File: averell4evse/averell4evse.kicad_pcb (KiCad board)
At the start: 2 copper layers, 91 x 78 mm, 43 parts, among them J1 Conn_01x16, J2 Conn_01x13, J3 Conn_01x04, J4 Conn_01x03, J5 Conn_01x09, U1 KT2520K-T, U2 NFCv4, U3 TLC5957RTQ, U4 74AUC2G125, U5 touch_sensor

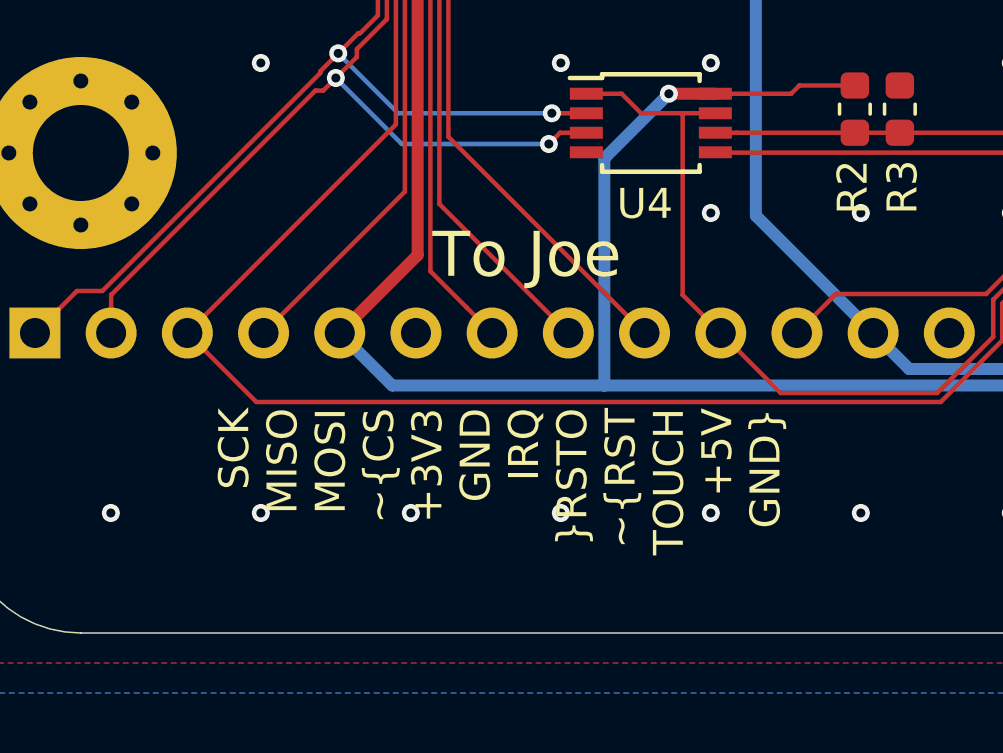
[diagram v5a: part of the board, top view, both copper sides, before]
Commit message: averell/pcb: Add DRV_CS to Joe connector silkscreen
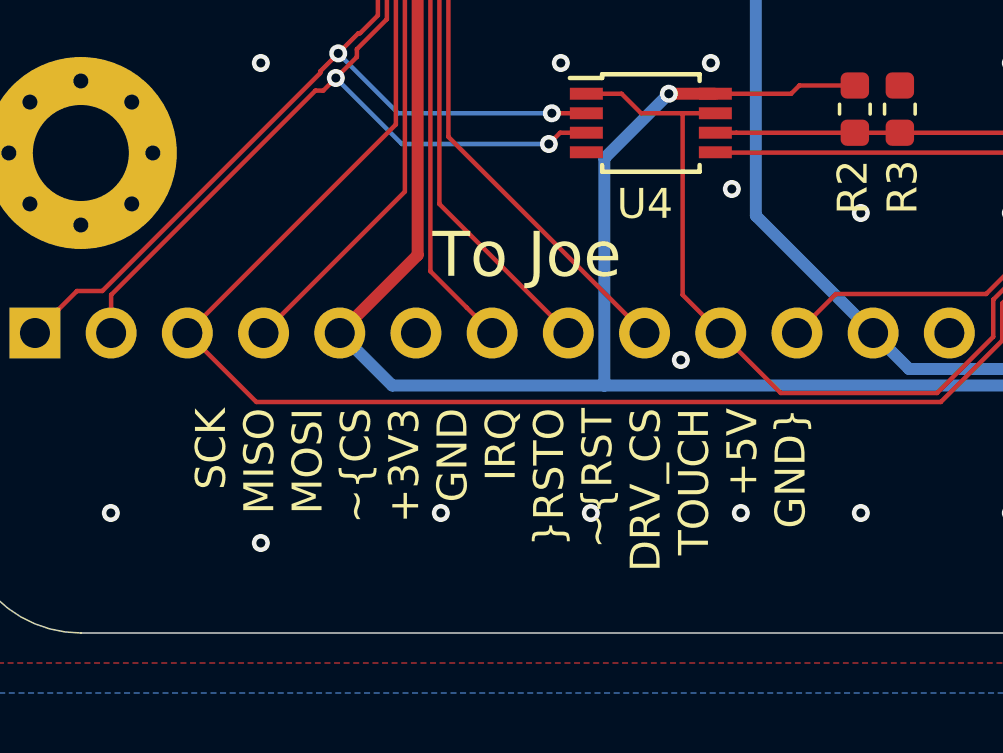
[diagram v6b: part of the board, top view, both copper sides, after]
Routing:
- net GND: vias 97 -> 98
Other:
- board text added: "SCK MISO MOSI ~CS +3V3 GND IRQ ~RSTO ~RST DRV_CS TOUCH +5V GND"
- board text removed: "SCK MISO MOSI ~CS +3V3 GND IRQ ~RSTO ~RST TOUCH +5V GND"
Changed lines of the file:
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@@
     (thickness 1.6)
     (drawings 35)
-    (tracks 1123)
+    (tracks 1124)
     (zones 0)
     (modules 44)
@@
     (effects (font (size 1 1) (thickness 0.15)) (justify right))
   )
-  (gr_text "SCK\nMISO\nMOSI\n~CS\n+3V3\nGND\nIRQ\n~RSTO\n~RST\nTOUCH\n+5V\nGND" (at 92.97 117.7 90) (layer B.SilkS)
+  (gr_text "SCK\nMISO\nMOSI\n~CS\n+3V3\nGND\nIRQ\n~RSTO\n~RST\nDRV_CS\nTOUCH\n+5V\nGND" (at 92.97 117.7 90) (layer B.SilkS)
     (effects (font (size 1 1) (thickness 0.15)) (justify right mirror))
   )
-  (gr_text "SCK\nMISO\nMOSI\n~CS\n+3V3\nGND\nIRQ\n~RSTO\n~RST\nTOUCH\n+5V\nGND" (at 92.97 121.5 90) (layer F.SilkS)
+  (gr_text "SCK\nMISO\nMOSI\n~CS\n+3V3\nGND\nIRQ\n~RSTO\n~RST\nDRV_CS\nTOUCH\n+5V\nGND" (at 93 121.5 90) (layer F.SilkS)
     (effects (font (size 1 1) (thickness 0.15)) (justify right))
   )
@@
   (via (at 146.17 115) (size 0.6) (drill 0.3) (layers F.Cu B.Cu) (net 1))
   (via (at 155.2 117) (size 0.6) (drill 0.3) (layers F.Cu B.Cu) (net 1))
-  (via (at 151.5 119.2) (size 0.6) (drill 0.3) (layers F.Cu B.Cu) (net 28))
   (via (at 150.5 94.6) (size 0.6) (drill 0.3) (layers F.Cu B.Cu) (net 1))
   (via (at 154.5 90.2) (size 0.6) (drill 0.3) (layers F.Cu B.Cu) (net 1))
@@
   (via (at 145 110) (size 0.6) (drill 0.3) (layers F.Cu B.Cu) (net 1))
   (via (at 140 110) (size 0.6) (drill 0.3) (layers F.Cu B.Cu) (net 1))
-  (via (at 100 115) (size 0.6) (drill 0.3) (layers F.Cu B.Cu) (net 1))
+  (via (at 100.7 114.2) (size 0.6) (drill 0.3) (layers F.Cu B.Cu) (net 1))
   (via (at 105 115) (size 0.6) (drill 0.3) (layers F.Cu B.Cu) (net 1))
   (via (at 110 115) (size 0.6) (drill 0.3) (layers F.Cu B.Cu) (net 1))
@@
   (via (at 165 120) (size 0.6) (drill 0.3) (layers F.Cu B.Cu) (net 1))
   (via (at 80 125) (size 0.6) (drill 0.3) (layers F.Cu B.Cu) (net 1))
-  (via (at 85 125) (size 0.6) (drill 0.3) (layers F.Cu B.Cu) (net 1))
-  (via (at 95 125) (size 0.6) (drill 0.3) (layers F.Cu B.Cu) (net 1))
-  (via (at 90 125) (size 0.6) (drill 0.3) (layers F.Cu B.Cu) (net 1))
-  (via (at 100 125) (size 0.6) (drill 0.3) (layers F.Cu B.Cu) (net 1))
+  (via (at 85 126) (size 0.6) (drill 0.3) (layers F.Cu B.Cu) (net 1))
+  (via (at 96 125) (size 0.6) (drill 0.3) (layers F.Cu B.Cu) (net 1))
+  (via (at 91 125) (size 0.6) (drill 0.3) (layers F.Cu B.Cu) (net 1))
+  (via (at 101 125) (size 0.6) (drill 0.3) (layers F.Cu B.Cu) (net 1))
   (via (at 105 125) (size 0.6) (drill 0.3) (layers F.Cu B.Cu) (net 1))
   (via (at 110 125) (size 0.6) (drill 0.3) (layers F.Cu B.Cu) (net 1))
@@
   (via (at 85 105) (size 0.6) (drill 0.3) (layers F.Cu B.Cu) (net 1))
   (via (at 85 110) (size 0.6) (drill 0.3) (layers F.Cu B.Cu) (net 1))
+  (via (at 99 119.9) (size 0.6) (drill 0.3) (layers F.Cu B.Cu) (net 1))
   (via (at 129 111.2) (size 0.6) (drill 0.3) (layers F.Cu B.Cu) (net 2))
   (segment (start 129 111.2) (end 129 112.2125) (width 0.4) (layer F.Cu) (net 2))
@@
   (segment (start 99.4 97.75) (end 99.925001 97.224999) (width 0.15) (layer B.Cu) (net 27))
   (segment (start 98.5 97.75) (end 99.4 97.75) (width 0.15) (layer B.Cu) (net 27))
+  (via (at 151.5 119.2) (size 0.6) (drill 0.3) (layers F.Cu B.Cu) (net 28))
   (segment (start 132.75 110.281602) (end 132.75 109.9375) (width 0.15) (layer F.Cu) (net 28))
   (segment (start 132.55001 110.481592) (end 132.75 110.281602) (width 0.15) (layer F.Cu) (net 28))
@@
   (segment (start 101.38 88.7) (end 99.2 90.88) (width 0.15) (layer F.Cu) (net 44))
   (segment (start 99.2 90.88) (end 99.2 91.794334) (width 0.15) (layer F.Cu) (net 44))
-  (via (at 130.25 99.6) (size 0.6) (drill 0.3) (layers F.Cu B.Cu) (net 77))
-  (segment (start 130.25 101.525) (end 130.25 99.6) (width 0.15) (layer F.Cu) (net 77))
-  (segment (start 130.25 102.0625) (end 130.25 101.525) (width 0.15) (layer F.Cu) (net 77))
   (via (at 130.775 100.157472) (size 0.6) (drill 0.3) (layers F.Cu B.Cu) (net 45))
   (segment (start 130.75 102.0625) (end 130.75 100.182472) (width 0.15) (layer F.Cu) (net 45))
@@
   (segment (start 87.5 110.5) (end 87.08 110.92) (width 0.15) (layer F.Cu) (net 46))
   (segment (start 87.08 110.92) (end 86.82 110.92) (width 0.15) (layer F.Cu) (net 46))
-  (via (at 129.725 100.176167) (size 0.6) (drill 0.3) (layers F.Cu B.Cu) (net 78))
-  (segment (start 129.75 102.0625) (end 129.75 100.201167) (width 0.15) (layer F.Cu) (net 78))
-  (segment (start 129.75 100.201167) (end 129.725 100.176167) (width 0.15) (layer F.Cu) (net 78))
-  (via (at 125.3 106.3) (size 0.6) (drill 0.3) (layers F.Cu B.Cu) (net 78))
-  (segment (start 125.3 106.3) (end 125.3 104.248443) (width 0.15) (layer B.Cu) (net 78))
-  (segment (start 125.3 104.248443) (end 129.024222 100.524221) (width 0.15) (layer B.Cu) (net 78))
-  (segment (start 129.376946 100.524221) (end 129.725 100.176167) (width 0.15) (layer B.Cu) (net 78))
-  (segment (start 129.024222 100.524221) (end 129.376946 100.524221) (width 0.15) (layer B.Cu) (net 78))
   (segment (start 93.76 95.9615) (end 93.76 88.7) (width 0.15) (layer F.Cu) (net 47))
   (segment (start 88.89999 100.821512) (end 88.901519 100.819981) (width 0.15) (layer F.Cu) (net 47))
@@
   (segment (start 96.535 64.5) (end 96.535 56.065) (width 0.15) (layer B.Cu) (net 76))
   (segment (start 96.535 56.065) (end 97.774989 54.825011) (width 0.15) (layer B.Cu) (net 76))
+  (via (at 130.25 99.6) (size 0.6) (drill 0.3) (layers F.Cu B.Cu) (net 77))
+  (segment (start 130.25 101.525) (end 130.25 99.6) (width 0.15) (layer F.Cu) (net 77))
+  (segment (start 130.25 102.0625) (end 130.25 101.525) (width 0.15) (layer F.Cu) (net 77))
   (segment (start 99.06 111.675) (end 100.15 111.675) (width 0.15) (layer F.Cu) (net 77))
   (segment (start 130.25 99.6) (end 129.524165 99.6) (width 0.15) (layer B.Cu) (net 77))
@@
   (segment (start 99.06 117.73) (end 99.06 111.675) (width 0.15) (layer F.Cu) (net 77))
   (segment (start 100.33 119) (end 99.06 117.73) (width 0.15) (layer F.Cu) (net 77))
+  (via (at 129.725 100.176167) (size 0.6) (drill 0.3) (layers F.Cu B.Cu) (net 78))
+  (segment (start 129.75 102.0625) (end 129.75 100.201167) (width 0.15) (layer F.Cu) (net 78))
+  (segment (start 129.75 100.201167) (end 129.725 100.176167) (width 0.15) (layer F.Cu) (net 78))
+  (via (at 125.3 106.3) (size 0.6) (drill 0.3) (layers F.Cu B.Cu) (net 78))
+  (segment (start 125.3 106.3) (end 125.3 104.248443) (width 0.15) (layer B.Cu) (net 78))
+  (segment (start 125.3 104.248443) (end 129.024222 100.524221) (width 0.15) (layer B.Cu) (net 78))
+  (segment (start 129.376946 100.524221) (end 129.725 100.176167) (width 0.15) (layer B.Cu) (net 78))
+  (segment (start 129.024222 100.524221) (end 129.376946 100.524221) (width 0.15) (layer B.Cu) (net 78))
   (segment (start 100.85 112.325) (end 104.8 112.325) (width 0.15) (layer F.Cu) (net 78))
   (segment (start 100.15 112.325) (end 100.85 112.325) (width 0.15) (layer F.Cu) (net 78))

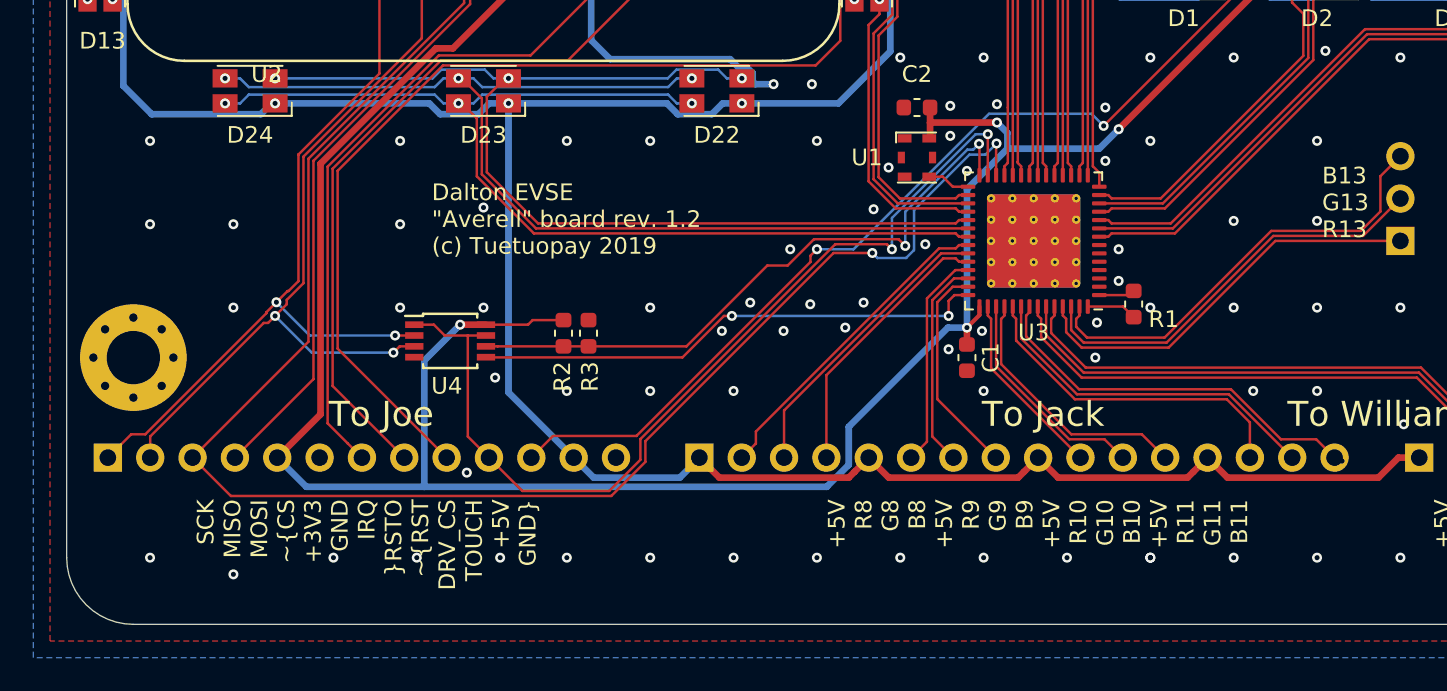
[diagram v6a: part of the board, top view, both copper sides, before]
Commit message: averell/pcb: Replace Joe connector with RJ45 jacks
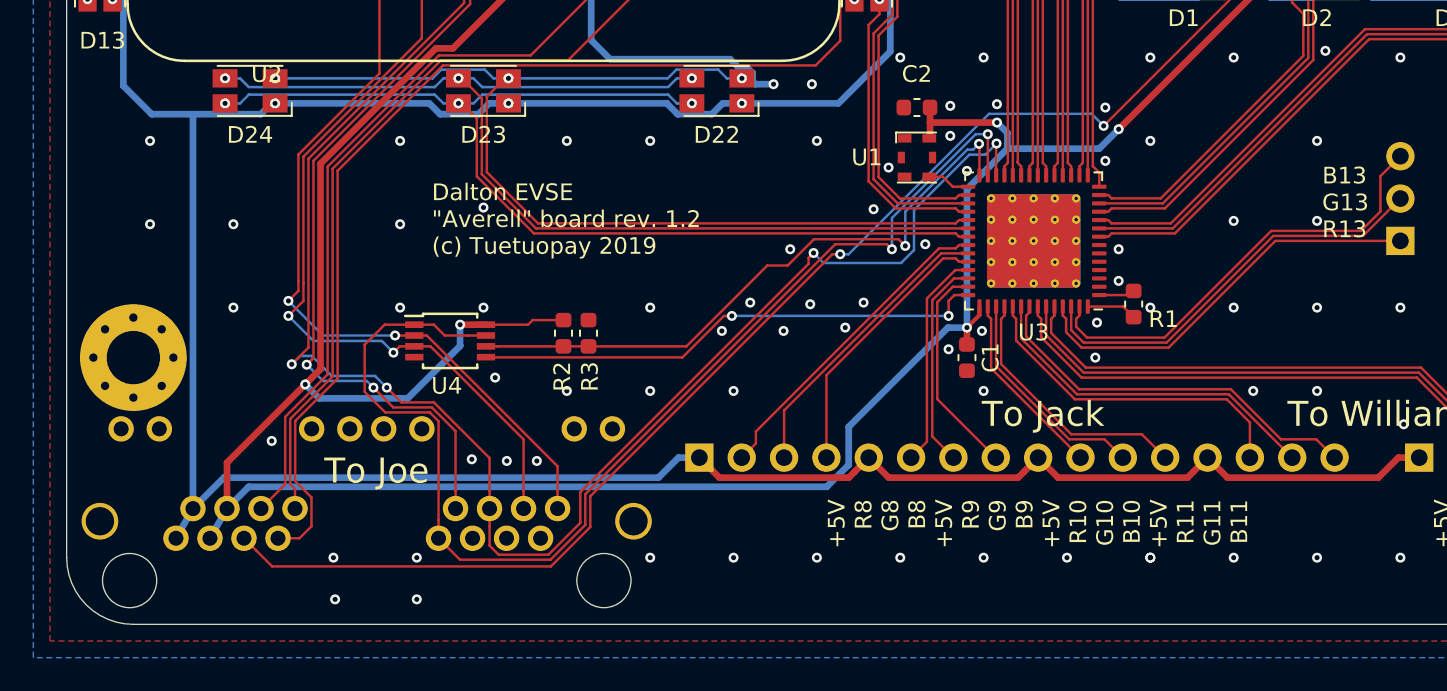
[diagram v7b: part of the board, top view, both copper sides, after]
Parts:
- J2: value Conn_01x13 -> CONNFLY_Elec_DS1129-04-S8B0P-X; footprint Connector_PinHeader_2.54mm:PinHeader_1x13_P2.54mm_Horizontal -> ma4evse:CONNFLY_Elec_DS1129-04-S8B0P-X
- moved J2 16.3 mm to (93.0, 124.0), turned to 180 degrees
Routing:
- net +5V: track 358.3 -> 384.2 mm
- net /TOUCH: track 61.8 -> 83.3 mm
- net /DRV_CS: track 56.6 -> 72.0 mm
- net +3V3: track 174.4 -> 185.2 mm, vias 4 -> 5
- net /NFC_CS: track 37.0 -> 44.9 mm, vias 0 -> 2
- net /~RST: track 94.6 -> 99.8 mm
- net /MOSI: track 99.3 -> 94.8 mm, vias 2 -> 4
- net /IRQ: track 42.0 -> 45.8 mm
- net /~RSTO: track 45.1 -> 47.5 mm
- net /SCK: track 46.7 -> 46.0 mm
- net GND: vias 98 -> 99
- net /B11: vias 1 -> 0
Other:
- board text removed: "SCK MISO MOSI ~CS +3V3 GND IRQ ~RSTO ~RST DRV_CS TOUCH +5V GND"

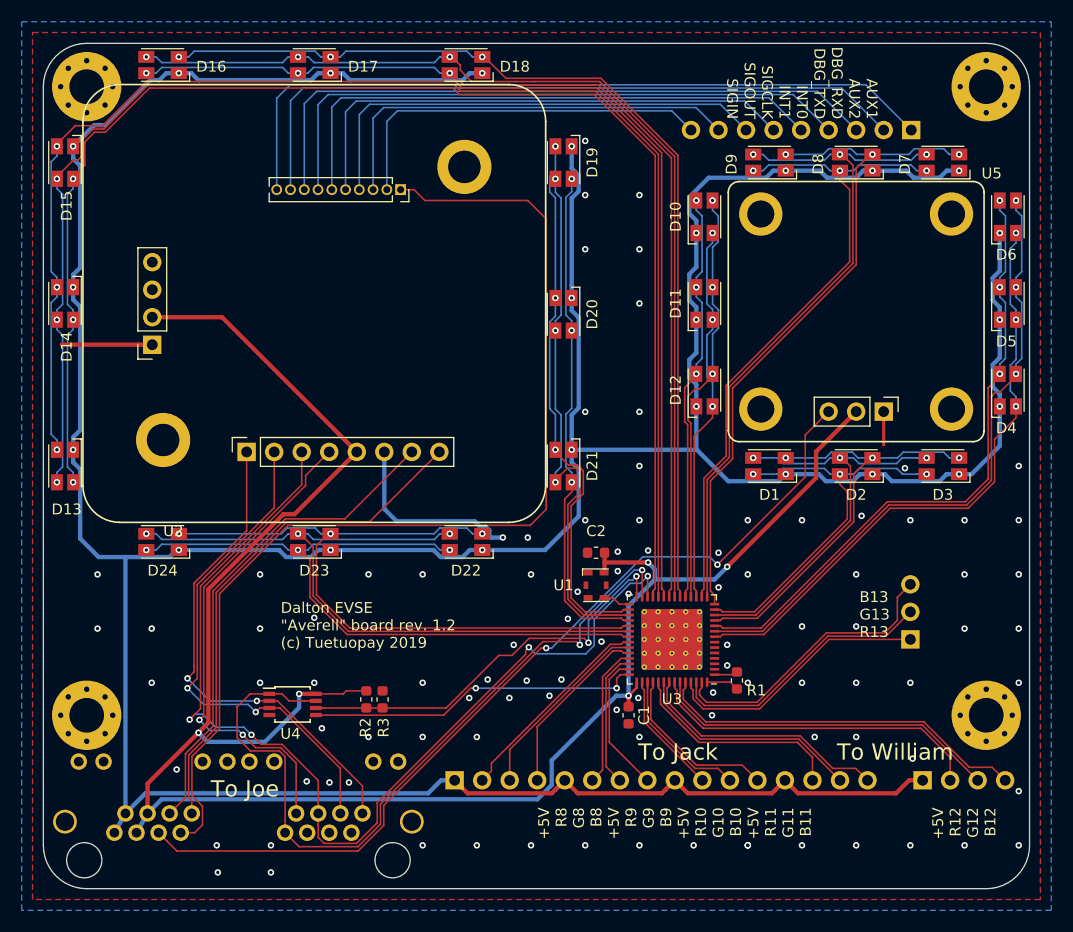
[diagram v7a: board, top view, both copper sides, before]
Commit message: averell/pcb: Move RJ45 connector and mounting screws backwards
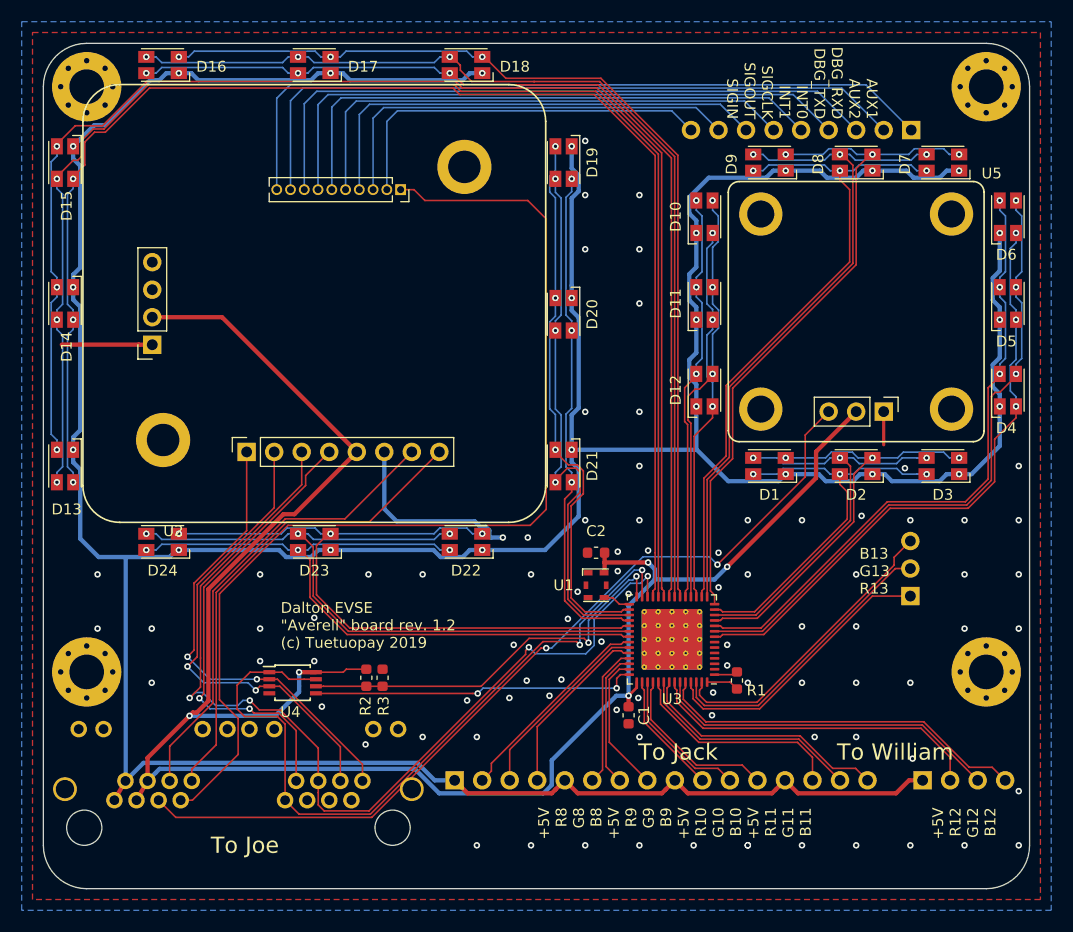
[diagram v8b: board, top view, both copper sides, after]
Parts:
- removed the REF** at (79.0, 113.0)
- removed the REF** at (162.0, 113.0)
- added REF**: MountingHole_3.2mm_M3_Pad_Via, MountingHole:MountingHole_3.2mm_M3_Pad_Via, F.Cu at (79.0, 109.0)
- added REF**: MountingHole_3.2mm_M3_Pad_Via, MountingHole:MountingHole_3.2mm_M3_Pad_Via, F.Cu at (162.0, 109.0)
- moved J4 4.00 mm to (155.0, 102.0)
- moved J2 3.00 mm to (93.0, 121.0)
- moved R2 2.00 mm to (104.8, 109.5)
- moved R3 2.00 mm to (106.3, 109.5)
- moved U4 2.00 mm to (98.0, 110.0)
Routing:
- net /MOSI: track 94.8 -> 90.5 mm
- net /~RSTO: track 47.5 -> 44.3 mm
- net /DRV_CS: track 72.0 -> 68.9 mm
- net /SCK: track 46.0 -> 43.0 mm
- net /MISO: track 46.7 -> 43.7 mm
- net /IRQ: track 45.8 -> 42.8 mm
- net +5V: track 384.2 -> 381.3 mm
- net /~RST: track 99.8 -> 97.3 mm
- net /NFC_CS: track 44.9 -> 42.5 mm
- net /TOUCH: track 83.3 -> 80.9 mm
- net Net-(J4-Pad2): track 25.1 -> 26.7 mm
- net Net-(J4-Pad1): track 24.7 -> 26.4 mm
- net +3V3: track 185.2 -> 183.7 mm
- net Net-(J2-PadA9): track 0.00 -> 0.99 mm
- net Net-(J4-Pad3): track 26.8 -> 27.6 mm
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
